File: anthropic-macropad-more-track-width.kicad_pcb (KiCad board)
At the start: 2 copper layers, 136 x 81 mm, 12 parts, among them SW1 ESC, SW10 ENTER, SW11 MIC, SW2 TAB, SW3 ALLOW_ONCE, SW4 UP, SW5 ALLOW_ALWAYS, SW6 LEFT, SW7 DOWN, SW8 RIGHT, SW9 REJECT, U1 XIAO_RP2040

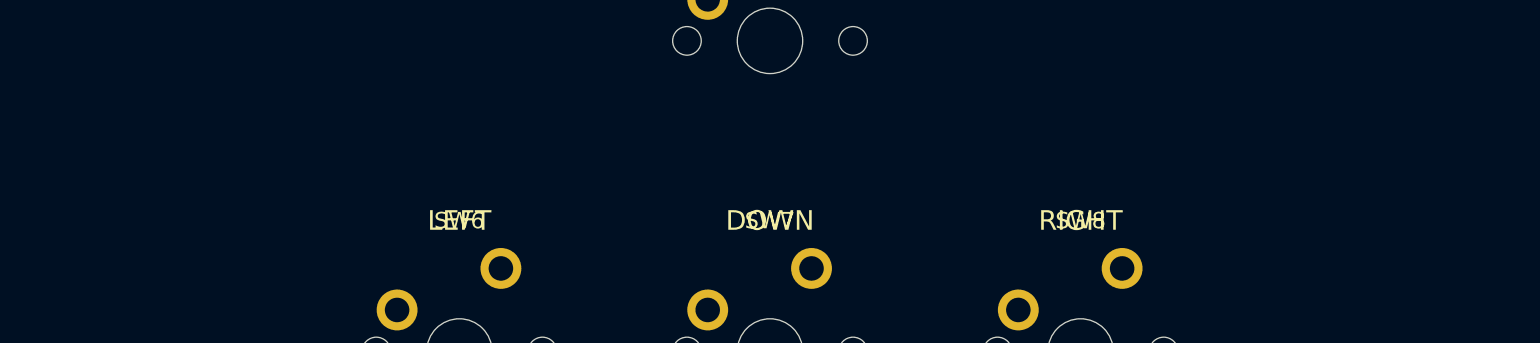
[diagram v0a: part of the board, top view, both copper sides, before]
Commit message: Add M2 mounting holes to wider-track variant
Co-Authored-By: Claude Opus 4.6 <noreply@anthropic.com>
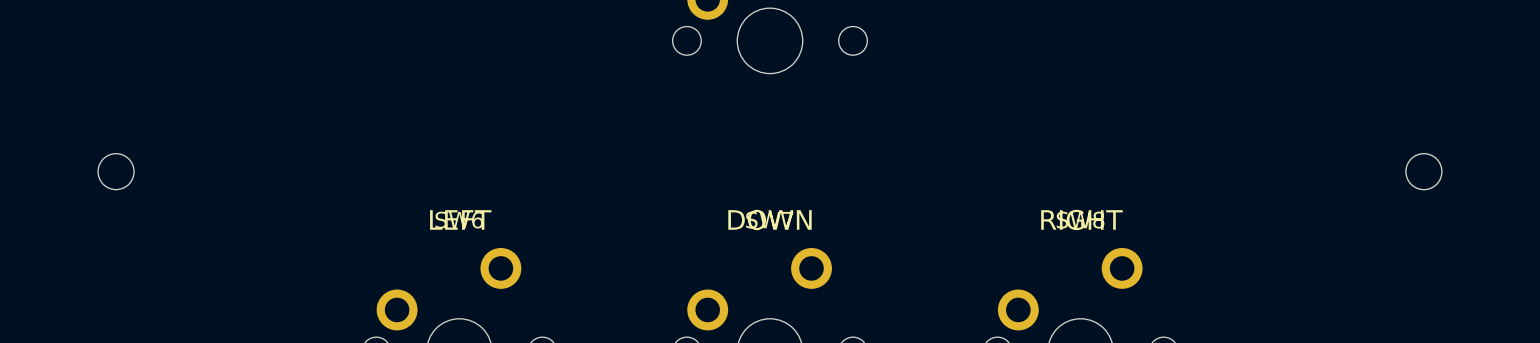
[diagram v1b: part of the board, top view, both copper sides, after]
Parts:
- added ?: , MountingHole:MountingHole_2.2mm_M2, F.Cu at (60.0, 68.0)
- added ?: , MountingHole:MountingHole_2.2mm_M2, F.Cu at (140.0, 68.0)
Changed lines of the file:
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@@
     (fp_text user "XIAO\nRP2040" (at 0 0 0) (layer "F.SilkS") (effects (font (size 1.5 1.5) (thickness 0.2))))
   )
+  (footprint "MountingHole:MountingHole_2.2mm_M2" (layer "F.Cu")
+    (at 60 68)
+    (descr "Mounting Hole 2.2mm M2")
+    (attr exclude_from_pos_files exclude_from_bom)
+    (pad "" np_thru_hole circle (at 0 0) (size 2.2 2.2) (drill 2.2) (layers "*.Cu" "*.Mask"))
+  )
+  (footprint "MountingHole:MountingHole_2.2mm_M2" (layer "F.Cu")
+    (at 140 68)
+    (descr "Mounting Hole 2.2mm M2")
+    (attr exclude_from_pos_files exclude_from_bom)
+    (pad "" np_thru_hole circle (at 0 0) (size 2.2 2.2) (drill 2.2) (layers "*.Cu" "*.Mask"))
+  )
 )

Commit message: Add GND copper pour on B.Cu and fill zones (pre-autoroute)
Co-Authored-By: Claude Opus 4.6 <noreply@anthropic.com>
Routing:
- added copper zone on B.Cu, net GND

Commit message: Add reference designators H1/H2 to mounting holes for DSN export
Co-Authored-By: Claude Opus 4.6 <noreply@anthropic.com>
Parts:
- gave numbers to parts that had none: 2
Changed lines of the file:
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@@
 		(at 140 68)
 		(descr "Mounting Hole 2.2mm M2")
-		(property "Reference" ""
+		(property "Reference" "H1"
 			(at 0 0 0)
 			(layer "F.SilkS")
@@
 		(at 60 68)
 		(descr "Mounting Hole 2.2mm M2")
-		(property "Reference" ""
-			(at 0 0 0)
-			(layer "F.SilkS")
+		(property "Reference" "H2"
+			(at 0 0 0)
+			(layer "F.SilkS")

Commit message: Autoroute wider-track variant via Freerouting
Co-Authored-By: Claude Opus 4.6 <noreply@anthropic.com>
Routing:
- net SW_REJECT: track 0.00 -> 91.5 mm, vias 0 -> 1
- net SW_ALLOW_ALWAYS: track 0.00 -> 76.6 mm
- net SW_MIC: track 0.00 -> 70.9 mm
- net SW_ALLOW_ONCE: track 0.00 -> 68.5 mm, vias 0 -> 1
- net SW_ENTER: track 0.00 -> 60.6 mm
- net SW_RIGHT: track 0.00 -> 39.7 mm
- net SW_LEFT: track 0.00 -> 32.5 mm
- net SW_DOWN: track 0.00 -> 30.8 mm
- net SW_UP: track 0.00 -> 19.1 mm
- net SW_ESC: track 0.00 -> 17.5 mm
